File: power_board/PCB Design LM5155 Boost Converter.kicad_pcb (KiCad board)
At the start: 2 copper layers, 80 x 53.2 mm, 35 parts, among them Q1 BSC035N04LS G, U1 LM5155_DSSR

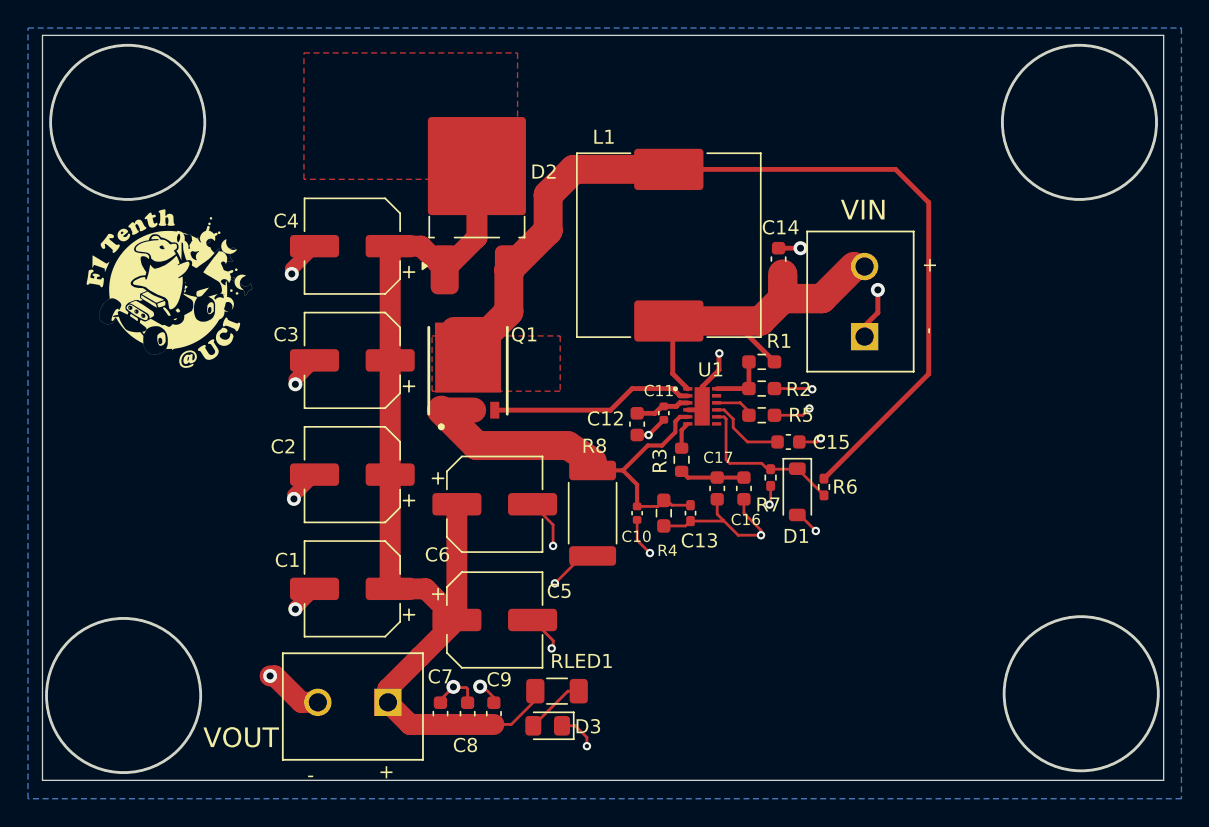
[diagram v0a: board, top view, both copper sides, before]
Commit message: Updated PCB Schematic
Moved the LM5155 to the right
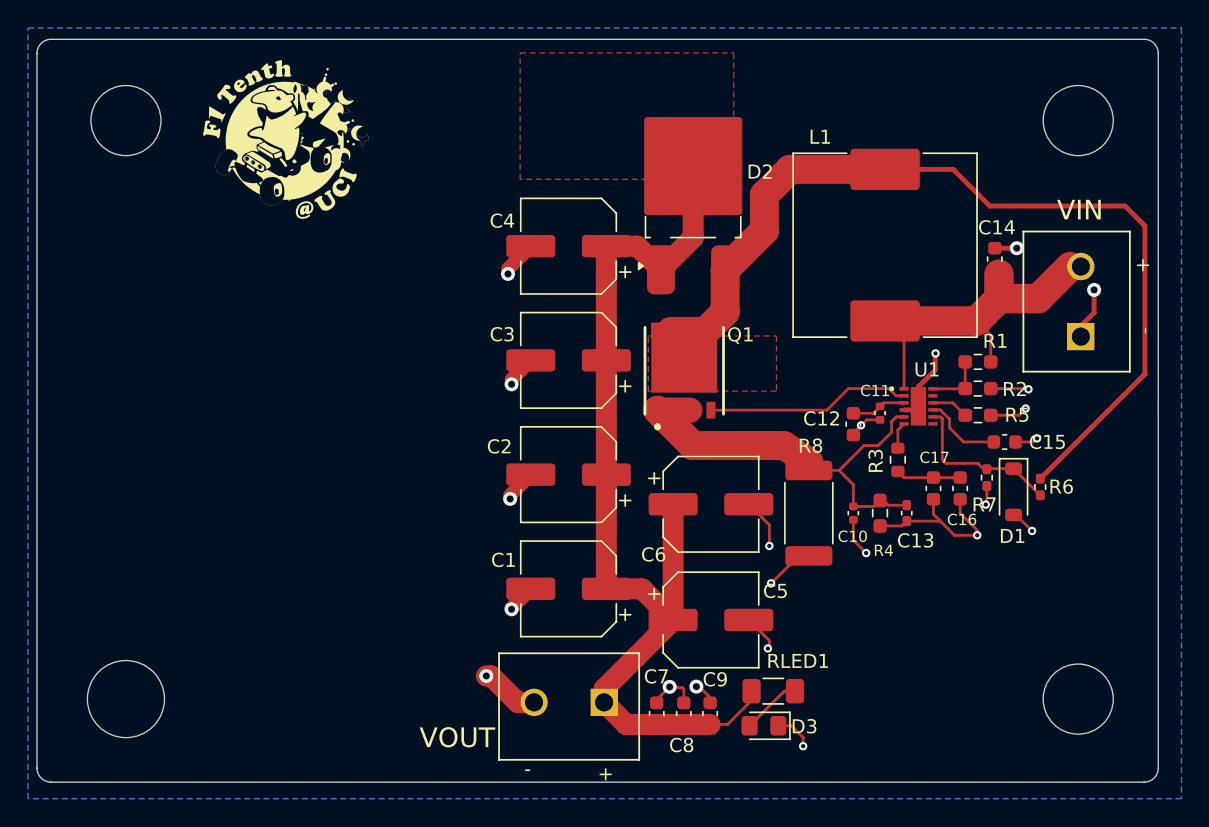
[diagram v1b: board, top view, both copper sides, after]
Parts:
- added REF**: MountingHole_5mm, MountingHole:MountingHole_5mm, F.Cu at (176.5, 57.1)
- added REF**: MountingHole_5.5mm, MountingHole:MountingHole_5.5mm, F.Cu at (108.6, 98.4)
- added REF**: MountingHole_5mm, MountingHole:MountingHole_5mm, F.Cu at (108.6, 57.1)
- added REF**: MountingHole_5mm, MountingHole:MountingHole_5mm, F.Cu at (176.5, 98.4)
- moved L1 15.4 mm to (162.7, 66.0)
- moved R1 15.4 mm to (169.4, 74.4)
- moved R2 15.4 mm to (169.4, 76.3)
- moved R3 15.4 mm to (163.7, 81.3)
- moved R5 15.4 mm to (169.4, 78.2)
- moved VIN 15.4 mm to (176.7, 72.6)
- moved C1 15.4 mm to (140.2, 90.6)
- moved C2 15.4 mm to (140.2, 82.4)
- moved C3 15.4 mm to (140.2, 74.3)
- moved C4 15.4 mm to (140.2, 66.1)
- moved C10 15.4 mm to (160.5, 85.2)
- moved C11 15.4 mm to (162.4, 78.0)
- moved C12 15.4 mm to (160.5, 78.8)
- moved C13 15.4 mm to (164.3, 85.2)
- moved C14 15.4 mm to (170.6, 67.0)
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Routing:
- net /Q1_DRAIN: track 65.2 -> 64.2 mm
- net /INDUCTOR: track 30.5 -> 29.5 mm
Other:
- board size 80 x 53.2 mm -> 80 x 53 mm

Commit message: Routing for TPS Module
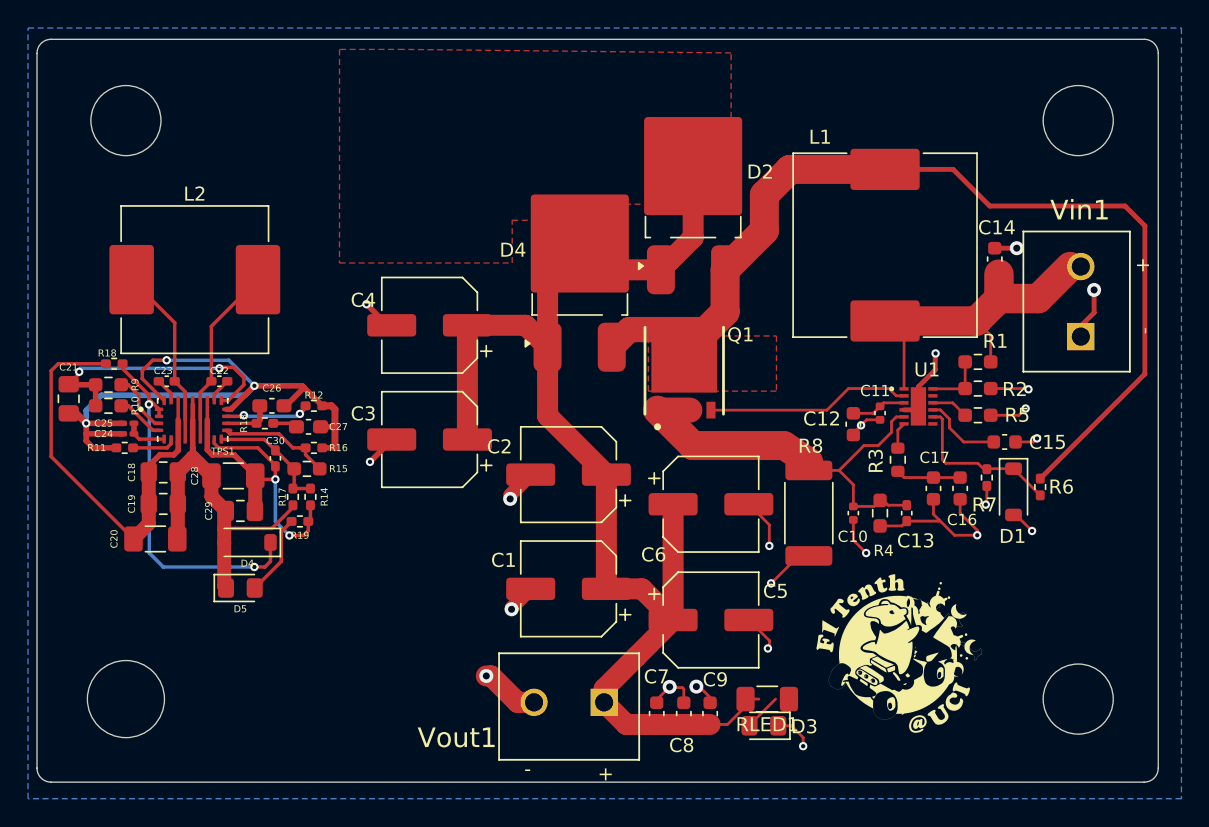
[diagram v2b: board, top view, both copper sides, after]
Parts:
- added C18: 10u, Capacitor_SMD:C_0805_2012Metric_Pad1.18x1.45mm_HandSolder, F.Cu at (111.2, 82.2)
- added C19: 10u, Capacitor_SMD:C_0805_2012Metric_Pad1.18x1.45mm_HandSolder, F.Cu at (111.2, 84.5)
- added C20: 22u, Capacitor_SMD:C_1206_3216Metric_Pad1.33x1.80mm_HandSolder, F.Cu at (110.7, 87.0)
- added C21: 4.7u, Capacitor_SMD:C_0805_2012Metric_Pad1.18x1.45mm_HandSolder, F.Cu at (104.5, 77.0)
- added C22: 0.1u, Capacitor_SMD:C_0402_1005Metric_Pad0.74x0.62mm_HandSolder, F.Cu at (115.2, 75.8)
- added C23: 0.1u, Capacitor_SMD:C_0402_1005Metric_Pad0.74x0.62mm_HandSolder, F.Cu at (111.5, 75.8)
- added C24: 470p, Capacitor_SMD:C_0201_0603Metric_Pad0.64x0.40mm_HandSolder, F.Cu at (108.8, 79.5)
- added C25: 6.8nF, Capacitor_SMD:C_0201_0603Metric_Pad0.64x0.40mm_HandSolder, F.Cu at (108.8, 78.8)
- added C26: 100p, Capacitor_SMD:C_0603_1608Metric_Pad1.08x0.95mm_HandSolder, F.Cu at (119.0, 77.5)
- added C27: 4.7n, Capacitor_SMD:C_0603_1608Metric_Pad1.08x0.95mm_HandSolder, F.Cu at (121.6, 79.0)
- added C28: 22u, Capacitor_SMD:C_1206_3216Metric_Pad1.33x1.80mm_HandSolder, F.Cu at (116.2, 82.5)
- added C29: 47u, Capacitor_SMD:C_0805_2012Metric_Pad1.18x1.45mm_HandSolder, F.Cu at (116.8, 85.0)
- added C30: 0.1u, Capacitor_SMD:C_0402_1005Metric_Pad0.74x0.62mm_HandSolder, F.Cu at (119.2, 81.2)
- added D4: D_Schottky, Package_TO_SOT_SMD:TO-252-2_TabPin1, F.Cu at (141.0, 67.9)
- added D4: 3.3, Diode_SMD:D_SOD-123, F.Cu at (117.2, 87.2)
- added D5: LED, LED_SMD:LED_0805_2012Metric_Pad1.15x1.40mm_HandSolder, F.Cu at (116.8, 90.5)
- added L2: 4.7u, Inductor_SMD:L_Vishay_IHLP-4040, F.Cu at (113.5, 68.5)
- added R10: 100k, Resistor_SMD:R_0603_1608Metric_Pad0.98x0.95mm_HandSolder, F.Cu at (107.3, 77.5)
- added R11: 50k, Resistor_SMD:R_0402_1005Metric_Pad0.72x0.64mm_HandSolder, F.Cu at (108.5, 80.5)
- added R12: 150k, Resistor_SMD:R_0402_1005Metric_Pad0.72x0.64mm_HandSolder, F.Cu at (122.0, 77.5)
- added R13: 10k, Resistor_SMD:R_0402_1005Metric_Pad0.72x0.64mm_HandSolder, F.Cu at (118.5, 78.8)
- added R14: 10m, Resistor_SMD:R_0402_1005Metric_Pad0.72x0.64mm_HandSolder, F.Cu at (121.8, 84.0)
- added R15: 100k, Resistor_SMD:R_0603_1608Metric_Pad0.98x0.95mm_HandSolder, F.Cu at (121.5, 82.0)
- added R16: 11k, Resistor_SMD:R_0402_1005Metric_Pad0.72x0.64mm_HandSolder, F.Cu at (122.0, 80.5)
- added R17: 3, Resistor_SMD:R_0402_1005Metric_Pad0.72x0.64mm_HandSolder, F.Cu at (120.5, 84.0)
- added R18: 3.3k, Resistor_SMD:R_0402_1005Metric_Pad0.72x0.64mm_HandSolder, F.Cu at (107.8, 74.5)
- added R19: 1k, Resistor_SMD:R_0402_1005Metric_Pad0.72x0.64mm_HandSolder, F.Cu at (121.0, 85.8)
- added R9: 100k, Resistor_SMD:R_0603_1608Metric_Pad0.98x0.95mm_HandSolder, F.Cu at (107.3, 76.0)
- added TPS1: ~, TPS552892RYQR:CONV_TPS552892RYQR, F.Cu at (113.3, 78.5)
- moved Ref 57.1 mm to (164.5, 95.2)
- moved C3 11.4 mm to (130.2, 79.9)
- moved C4 11.4 mm to (130.2, 71.8)
- moved RLED1 0.71 mm to (154.3, 98.4)
- renumbered VIN to Vin1, VOUT to Vout1
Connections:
- C14 pad 1: /INDUCTOR -> Net-(U1-BIAS)
- D2 pad 2: /Q1_DRAIN -> /INDUCTOR
- L1 pad 1: /INDUCTOR -> Net-(U1-BIAS)
- L1 pad 2: /Q1_DRAIN -> /INDUCTOR
- Q1 pad 5: /Q1_DRAIN -> /INDUCTOR
- Q1 pad 6: /Q1_DRAIN -> /INDUCTOR
- Q1 pad 7: /Q1_DRAIN -> /INDUCTOR
- Q1 pad 8: /Q1_DRAIN -> /INDUCTOR
- R1 pad 2: /INDUCTOR -> Net-(U1-BIAS)
- R6 pad 1: /Q1_DRAIN -> /INDUCTOR
- U1 pad 1: /INDUCTOR -> Net-(U1-BIAS)
- Vin1 pad 2: /INDUCTOR -> Net-(U1-BIAS)
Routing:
- net GND: track 69.9 -> 121.3 mm, vias 22 -> 25
- net /COUT: track 71.8 -> 120.9 mm
- net /INDUCTOR: track 29.5 -> 0.00 mm
- net Net-(D4-K): track 0.00 -> 26.8 mm, vias 0 -> 2
- net PGND: track 0.00 -> 25.7 mm
- net Net-(U1-BIAS): track 0.00 -> 25.3 mm
- net /VOUT: track 0.00 -> 24.5 mm, vias 0 -> 2
- net Net-(TPS1-VCC): track 0.00 -> 19.5 mm, vias 0 -> 2
- net Net-(TPS1-SW2): track 0.00 -> 11.7 mm
- net Net-(TPS1-SW1): track 0.00 -> 11.6 mm
- net Net-(TPS1-FB): track 0.00 -> 8.81 mm
- net Net-(TPS1-ISN): track 0.00 -> 8.77 mm
- net Net-(TPS1-CDC): track 0.00 -> 6.13 mm, vias 0 -> 2
- net Net-(D5-A): track 0.00 -> 5.84 mm
- net /Q1_DRAIN: track 64.2 -> 68.9 mm
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- added copper zone on F.Cu, net /INDUCTOR
- removed copper zone on F.Cu, net /Q1_DRAIN

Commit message: PCB Traces
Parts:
- added NT1: NetTie_2, NetTie:NetTie-2_SMD_Pad0.5mm, F.Cu at (108.2, 84.8)
- added NT2: NetTie_2, NetTie:NetTie-2_SMD_Pad0.5mm, F.Cu at (123.0, 78.0)
- added R20: 0, Resistor_SMD:R_0402_1005Metric_Pad0.72x0.64mm_HandSolder, F.Cu at (108.8, 90.1)
- moved D4 15.3 mm to (106.3, 76.5)
- moved R17 6.00 mm to (123.5, 89.2), turned to 0 degrees
- moved R15 4.95 mm to (124.3, 86.0), turned to 90 degrees
- moved C30 4.74 mm to (122.3, 84.9), turned to 0 degrees
- moved C25 4.66 mm to (110.9, 82.9)
- moved R18 4.47 mm to (110.7, 77.9)
- moved R10 4.38 mm to (110.1, 80.9)
- moved R9 4.30 mm to (110.1, 79.3)
- moved R14 4.12 mm to (122.3, 88.1), turned to 0 degrees
- moved C23 4.10 mm to (114.2, 78.8)
- moved R19 4.03 mm to (119.4, 89.5), turned to 0 degrees
- moved C18 4.01 mm to (113.7, 85.4)
- moved C19 4.01 mm to (113.7, 87.7)
- moved R11 3.95 mm to (110.7, 83.8)
- moved C20 3.93 mm to (113.1, 90.1)
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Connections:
- C18 pad 2: PGND -> GND
- C21 pad 1: GND -> AGND
- C21 pad 2: Net-(TPS1-VCC) -> Net-(C21-Pad2)
- C24 pad 2: GND -> AGND
- C25 pad 2: GND -> AGND
- C26 pad 2: GND -> AGND
- C27 pad 2: GND -> AGND
- C28 pad 2: PGND -> GND
- C29 pad 2: PGND -> GND
- D4 pad 2: PGND -> GND
- D5 pad 1: PGND -> GND
- R11 pad 2: GND -> AGND
- R12 pad 2: GND -> AGND
- R16 pad 2: GND -> AGND
- R17 pad 2: PGND -> AGND
- TPS1 pad 17: GND -> AGND
- TPS1 pad 21: GND -> AGND
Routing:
- net GND: track 121.3 -> 93.9 mm, vias 25 -> 29
- net Net-(TPS1-VCC): track 19.5 -> 45.3 mm, vias 2 -> 0
- net PGND: track 25.7 -> 0.00 mm
- net AGND: track 0.00 -> 20.6 mm, vias 0 -> 13
- net Net-(D4-K): track 26.8 -> 8.27 mm, vias 2 -> 0
- net Net-(C21-Pad2): track 0.00 -> 10.2 mm
- net Net-(D5-A): track 5.84 -> 1.67 mm
- net /COUT: track 120.9 -> 124.9 mm
- net Net-(TPS1-ISN): track 8.77 -> 12.1 mm
- net Net-(TPS1-CDC): track 6.13 -> 3.16 mm, vias 2 -> 0
- net /VOUT: track 24.5 -> 22.2 mm, vias 2 -> 0
- net Net-(TPS1-SW2): track 11.7 -> 9.51 mm
- net Net-(TPS1-SW1): track 11.6 -> 9.50 mm
- net Net-(TPS1-FB): track 8.81 -> 7.36 mm
- net Net-(TPS1-CC): track 3.42 -> 2.92 mm
- added copper zone on B.Cu, net AGND
